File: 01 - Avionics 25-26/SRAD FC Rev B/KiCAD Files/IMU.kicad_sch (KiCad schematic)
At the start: 0 parts

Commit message: Added IMU and Barometer Circuits w/Root Symbols
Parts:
- added C4, C5, C6: 0.1uF, symbol Device:C_Small
- added U1: ICM-20948, QFN24_3X3X0P9_IVS, symbol 2025-11-06_05-57-26:ICM-20948
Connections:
- new net: C5.2, U1.10 (REGOUT)
- new net 1.71-1.95V: C4.2, C6.2, U1.13 (VDD), U1.8 (VDDIO)
- new net FSYNC: U1.11 (FSYNC)
- new net GND: C4.1, C5.1, C6.1, U1.18 (GND), U1.20 (RESV_GND)
- new net INT1: U1.12 (INT1)
- new net SCLK: U1.23 (SCL/SCLK)
- new net SDA: U1.24 (SDA/SDI)
- new net SDO: U1.9 (SDO/AD0)
- new net nCS: U1.22 (nCS)
- no-connect marks 0 -> 2

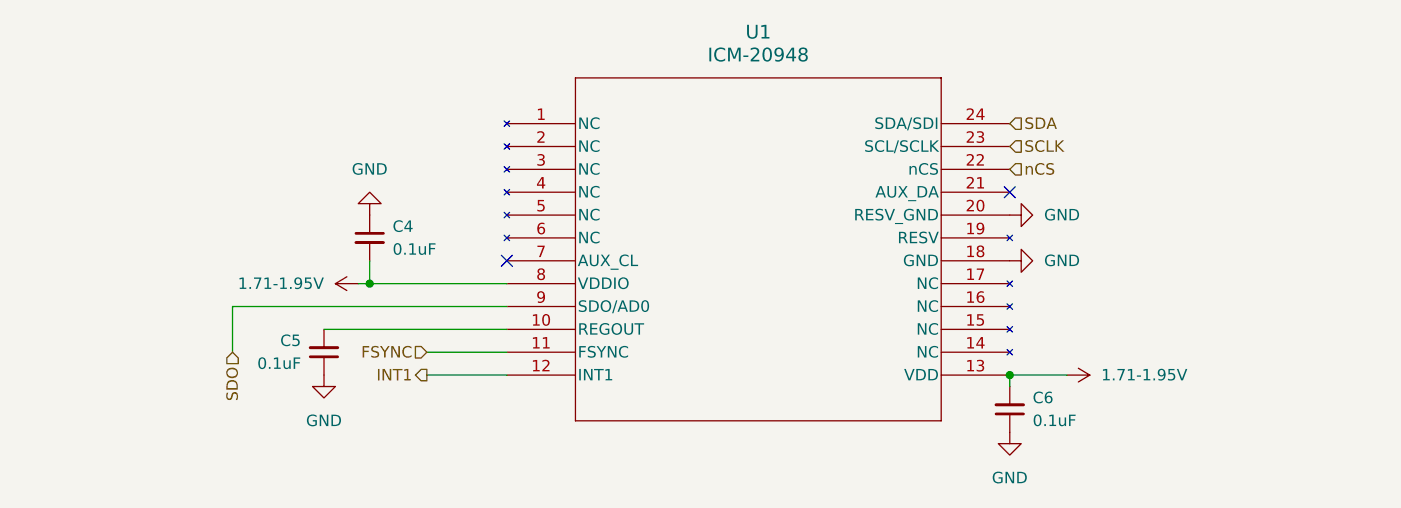
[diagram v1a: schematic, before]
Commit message: added power as hierarchical sheet pins
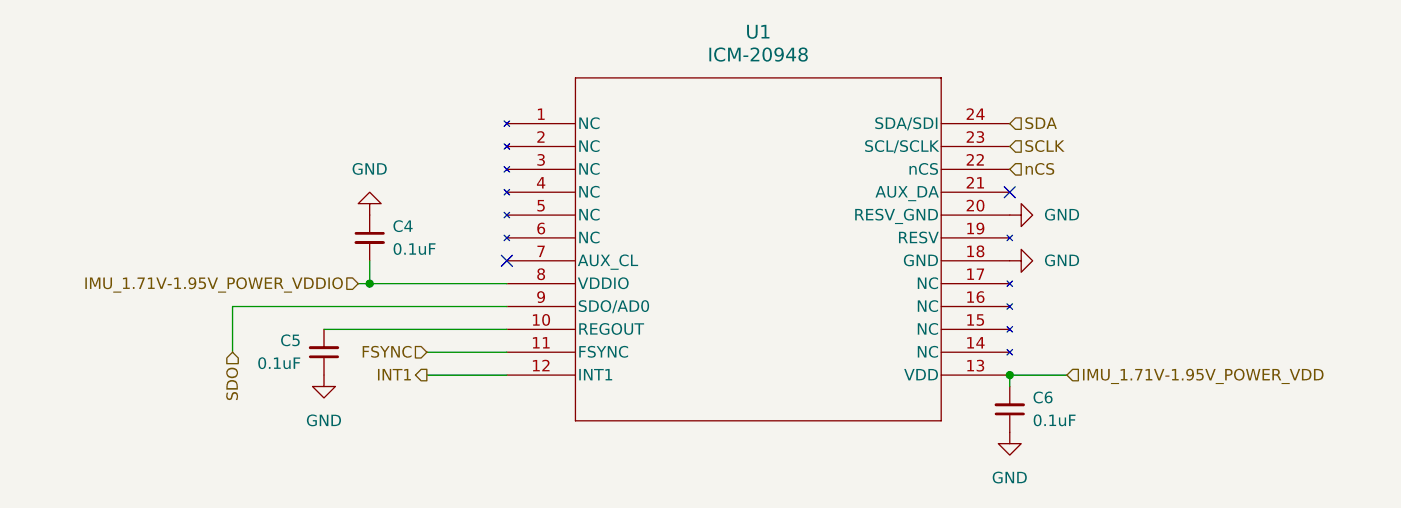
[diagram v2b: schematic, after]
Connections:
- net 1.71-1.95V renamed IMU_1.71V-1.95V_POWER_VDD
- net IMU_1.71V-1.95V_POWER_VDD: no longer C4.2, U1.8 (VDDIO)
- new net IMU_1.71V-1.95V_POWER_VDDIO: C4.2, U1.8 (VDDIO)
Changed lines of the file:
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@@
+		)
+	)
+	(hierarchical_label "IMU_1.71V-1.95V_POWER_VDD"
+		(shape input)
+		(at 181.61 110.49 0)
+		(effects
+			(font
+				(size 1.27 1.27)
+			)
+			(justify left)
 		)
 	)
@@
 		)
 	)
+	(hierarchical_label "IMU_1.71V-1.95V_POWER_VDDIO"
+		(shape input)
+		(at 102.87 100.33 180)
+		(effects
+			(font
+				(size 1.27 1.27)
+			)
+			(justify right)
+		)
+	)
 	(symbol
 		(lib_id "Device:C_Small")
@@
 	)
 	(symbol
-		(lib_id "power:+1V8")
-		(at 102.87 100.33 90)
-		(unit 1)
-		(exclude_from_sim no)
-		(in_bom yes)
-		(on_board yes)
-		(dnp no)
-		(fields_autoplaced yes)
-		(property "Reference" "#PWR06"
-			(at 106.68 100.33 0)
-			(effects
-				(font
-					(size 1.27 1.27)
-				)
-				(hide yes)
-			)
-		)
-		(property "Value" "1.71-1.95V"
-			(at 99.06 100.3299 90)
-			(effects
-				(font
-					(size 1.27 1.27)
-				)
-				(justify left)
-			)
-		)
-		(property "Footprint" ""
-			(at 102.87 100.33 0)
-			(effects
-				(font
-					(size 1.27 1.27)
-				)
-				(hide yes)
-			)
-		)
-		(property "Datasheet" ""
-			(at 102.87 100.33 0)
-			(effects
-				(font
-					(size 1.27 1.27)
-				)
-				(hide yes)
-			)
-		)
-		(property "Description" "Power symbol creates a global label with name \"+1V8\""
-			(at 102.87 100.33 0)
-			(effects
-				(font
-					(size 1.27 1.27)
-				)
-				(hide yes)
-			)
-		)
-		(pin "1"
-		)
-		(instances
-			(project ""
-				(path "/1dd9e63a-24f2-43c6-ae21-66b89e6998f2/d397a668-4bbe-408b-87ba-bb63aeafdd94"
-					(reference "#PWR06")
-					(unit 1)
-				)
-			)
-		)
-	)
-	(symbol
 		(lib_id "power:GND")
 		(at 99.06 110.49 0)
@@
 					(unit 1)
 				)
-			)
-		)
-	)
-	(symbol
-		(lib_id "power:+1V8")
-		(at 181.61 110.49 270)
-		(unit 1)
-		(exclude_from_sim no)
-		(in_bom yes)
-		(on_board yes)
-		(dnp no)
-		(fields_autoplaced yes)
-		(property "Reference" "#PWR011"
-			(at 177.8 110.49 0)
-			(effects
-				(font
-					(size 1.27 1.27)
-				)
-				(hide yes)
-			)
-		)
-		(property "Value" "1.71-1.95V"
-			(at 185.42 110.4899 90)
-			(effects
-				(font
-					(size 1.27 1.27)
-				)
-				(justify left)
-			)
-		)
-		(property "Footprint" ""
-			(at 181.61 110.49 0)
-			(effects
-				(font
-					(size 1.27 1.27)
-				)
-				(hide yes)
-			)
-		)
-		(property "Datasheet" ""
-			(at 181.61 110.49 0)
-			(effects
-				(font
-					(size 1.27 1.27)
-				)
-				(hide yes)
-			)
-		)
-		(property "Description" "Power symbol creates a global label with name \"+1V8\""
-			(at 181.61 110.49 0)
-			(effects
-				(font
-					(size 1.27 1.27)
-				)
-				(hide yes)
-			)
-		)
-		(pin "1"
-		)
-		(instances
-			(project "SRAD FC Rev B"
-				(path "/1dd9e63a-24f2-43c6-ae21-66b89e6998f2/d397a668-4bbe-408b-87ba-bb63aeafdd94"
-					(reference "#PWR011")
-					(unit 1)
-				)
